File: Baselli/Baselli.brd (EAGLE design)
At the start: 54 x 54 mm, 80 parts, among them J1 FTDI-SER-6-PP, J4 JTAG_PROG, Q1 8MHz NP, Q2 IRLML2244, SW1 A6H-2101, U1 STM32F051R, U4 LCMXO2-256HC-4SG32, X1 M-BOLT-2, X2 M-BOLT-2, X3 M-BOLT-2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

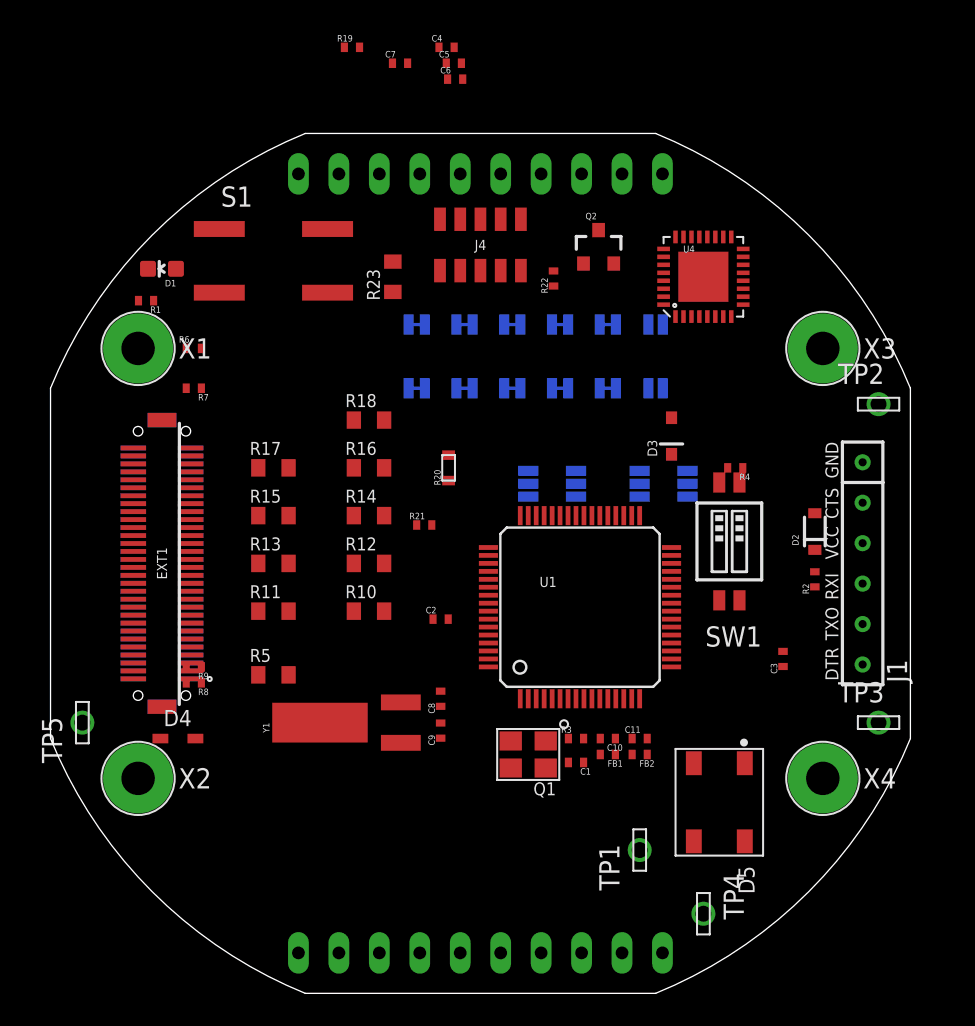
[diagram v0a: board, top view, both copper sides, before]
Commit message: Move components in Baselli layout, anticipating autorouter
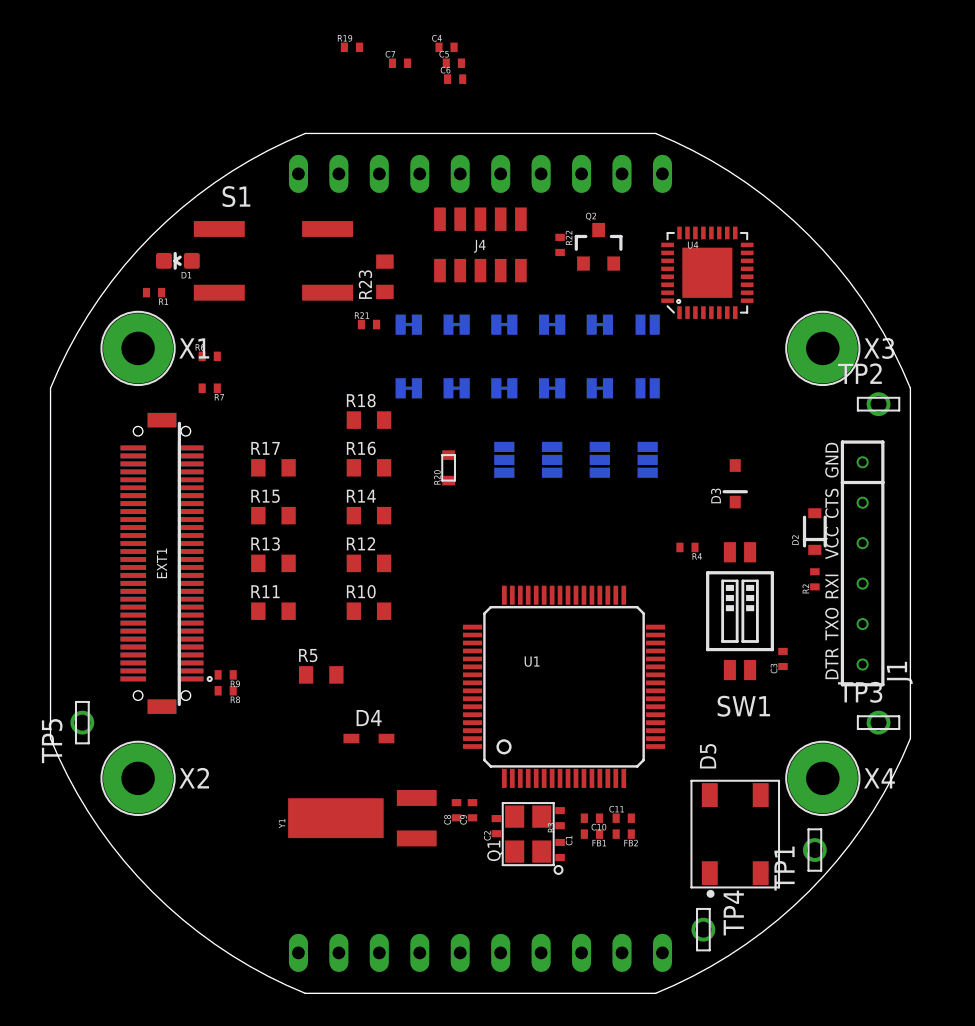
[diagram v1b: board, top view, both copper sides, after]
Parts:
- moved C2 13.5 mm to (28.0, 10.5), turned to 90 degrees
- moved R21 13.1 mm to (20.0, 42.0)
- moved D4 12.0 mm to (20.0, 16.0)
- moved TP1 11.0 mm to (48.0, 9.00)
- moved C8 7.07 mm to (25.5, 11.5)
- moved Y1 6.08 mm to (23.0, 11.0)
- moved R4 5.83 mm to (40.0, 28.0)
- moved C1 5.59 mm to (32.0, 9.00), turned to 270 degrees
- moved C9 5.39 mm to (26.5, 11.5)
- moved C10 5.10 mm to (34.0, 11.0)
- moved C11 5.10 mm to (36.0, 11.0)
- moved FB1 5.10 mm to (34.0, 10.0)
- moved FB2 5.10 mm to (36.0, 10.0)
- moved R3 5.10 mm to (32.0, 11.0), turned to 90 degrees
- moved U1 5.10 mm to (32.2, 19.2)
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
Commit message: Added layers.  Moved parts.
Per discussion between Pekka and Antti.
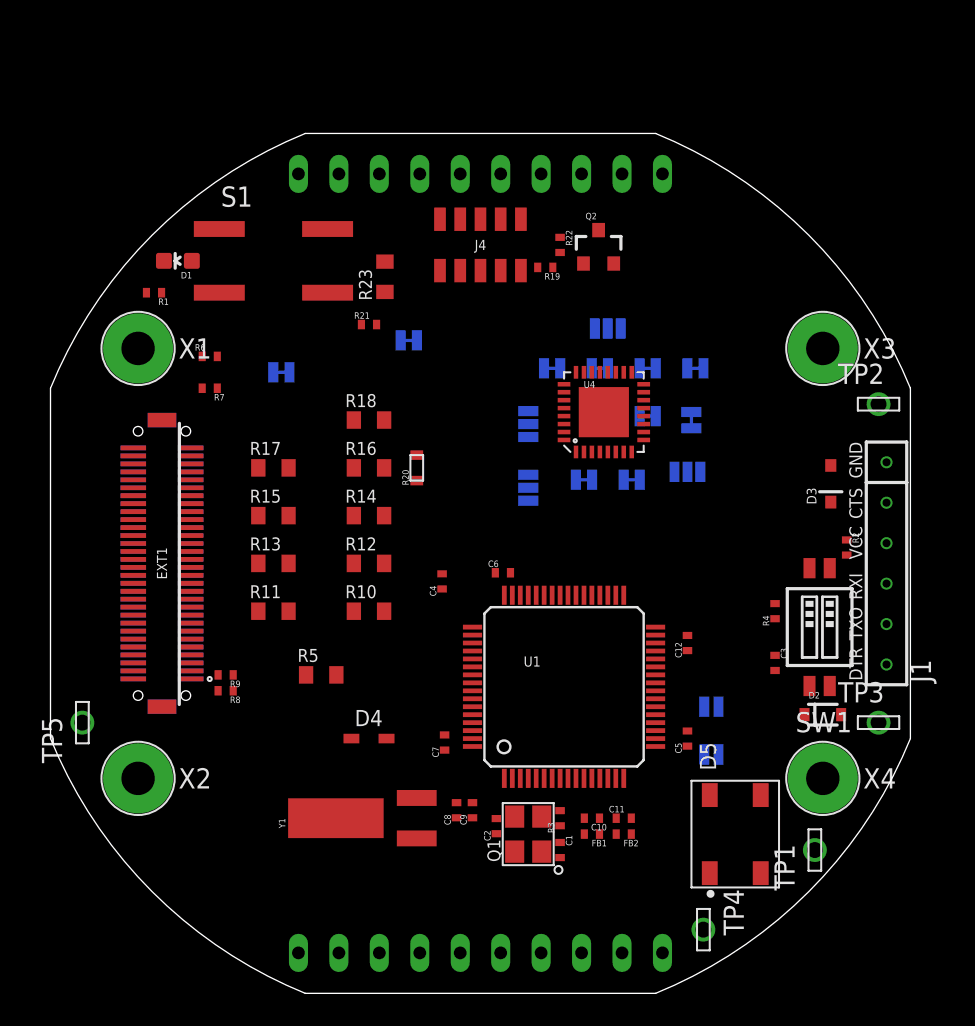
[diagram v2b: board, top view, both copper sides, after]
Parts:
- added C12: 100nF, ELL-i-Passives:C0402
- C4: value 1uF -> 4.7uF
- C6: value 1uF -> 100nF
- U1: value STM32F051R -> STM32F051R8T
- moved C5 44.9 mm to (40.0, 16.0), turned to 90 degrees
- moved C7 42.8 mm to (24.8, 15.8), turned to 90 degrees
- moved C4 33.5 mm to (24.6, 25.9), turned to 90 degrees
- moved C6 31.1 mm to (28.4, 26.4)
- moved SJ5 24.3 mm to (41.5, 18.0)
- moved SJ6 23.3 mm to (41.5, 15.0)
- moved R19 18.4 mm to (31.1, 45.6), turned to 180 degrees
- moved SJ13 12.6 mm to (33.5, 32.2)
- moved SJ14 12.4 mm to (36.5, 32.2)
- moved SJ11 12.3 mm to (40.5, 39.2)
- moved D2 11.5 mm to (48.5, 17.5), turned to 0 degrees
- moved U4 10.9 mm to (34.8, 36.5)
- moved SJ9 10.6 mm to (40.2, 36.0), turned to 90 degrees
- moved SJ12 9.09 mm to (37.5, 39.2)
- moved SJ2 8.96 mm to (35.0, 41.8), turned to 180 degrees
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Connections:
- net +3V3: now also C12.1
- net GNDI: now also C12.2
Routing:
- added copper zone on layer 15, net +3V3
- added copper zone on layer 2, net GNDI

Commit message: Add filter capacitors for Mach XO2 and initial routing for power
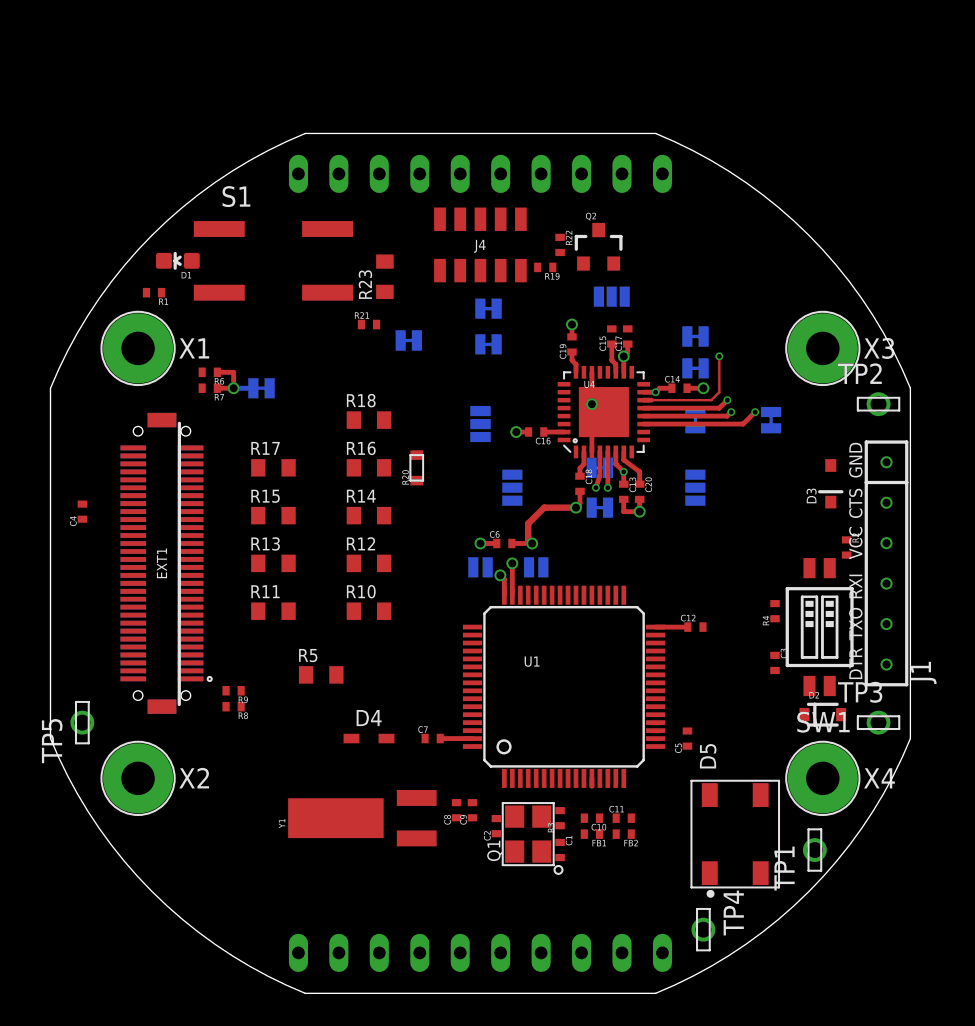
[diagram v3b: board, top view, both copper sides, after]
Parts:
- added C13, C14, C15, C16, C17, C18, C19, C20: 100nF, ELL-i-Passives:C0402
- moved C4 23.0 mm to (2.00, 30.2)
- moved SJ5 16.9 mm to (27.0, 26.8), turned to 180 degrees
- moved SJ6 16.1 mm to (30.5, 26.8)
- moved SJ7 7.94 mm to (27.5, 43.0), turned to 180 degrees
- moved SJ9 5.00 mm to (45.2, 36.0)
- moved SJ8 4.27 mm to (27.5, 40.8), turned to 180 degrees
- moved SJ12 3.61 mm to (40.5, 41.2), turned to 180 degrees
- moved SJ10 3.01 mm to (40.5, 36.0), turned to 90 degrees
- moved SJ1 3.00 mm to (27.0, 35.8)
- moved SJ14 2.66 mm to (34.5, 30.5), turned to 180 degrees
- moved SJ2 2.02 mm to (35.2, 43.8), turned to 0 degrees
- moved C6 1.84 mm to (28.5, 28.2)
- moved SJ16 1.60 mm to (13.2, 38.0)
- moved SJ13 1.25 mm to (34.5, 33.0), turned to 180 degrees
- moved C12 1.12 mm to (40.5, 23.0), turned to 0 degrees
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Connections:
- net +3V3: now also C17.1, C18.1
- net GNDI: now also C13.2, C14.2, C15.2, C16.2, C17.2, C18.2, C19.2, C20.2, U4.EP
- net N$1: now also C16.1, C19.1
- net N$2: now also C15.1
- net N$3: now also C14.1, C20.1
- net N$4: now also C13.1
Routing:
- net GNDI: track 0.00 -> 17.3 mm, vias 0 -> 7
- net +3V3: track 0.00 -> 10.8 mm, vias 0 -> 3
- net N$9: track 0.00 -> 7.31 mm, vias 0 -> 1
- net N$16: track 0.00 -> 7.21 mm, vias 0 -> 1
- net N$10: track 0.00 -> 5.60 mm, vias 0 -> 1
- net N$15: track 0.00 -> 5.46 mm, vias 0 -> 1
- net N$3: track 0.00 -> 4.40 mm, vias 0 -> 1
- net N$1: track 0.00 -> 2.65 mm
- net N$17: track 0.00 -> 2.29 mm, vias 0 -> 1
- net N$20: track 0.00 -> 2.25 mm, vias 0 -> 1
- net N$4: track 0.00 -> 2.25 mm, vias 0 -> 1
- net PF6: track 0.00 -> 2.00 mm, vias 0 -> 1
- net N$2: track 0.00 -> 1.88 mm
- net PF7: track 0.00 -> 1.35 mm, vias 0 -> 1
- net VSSA: track 0.00 -> 0.50 mm

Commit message: Add SJ17,18 to Baselli for SMT32L063 compatibility
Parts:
- added SJ17, SJ18: OPEN, SparkFun-Passives:SJ_2S-NO
- moved C5 2.24 mm to (41.0, 18.0), turned to 270 degrees
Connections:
- net +3V3: now also SJ17.1
- net GNDI: now also SJ18.1
- net PF4: now also SJ18.2
- net PF5: now also SJ17.2
